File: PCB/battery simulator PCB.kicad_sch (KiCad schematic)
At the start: 9 parts

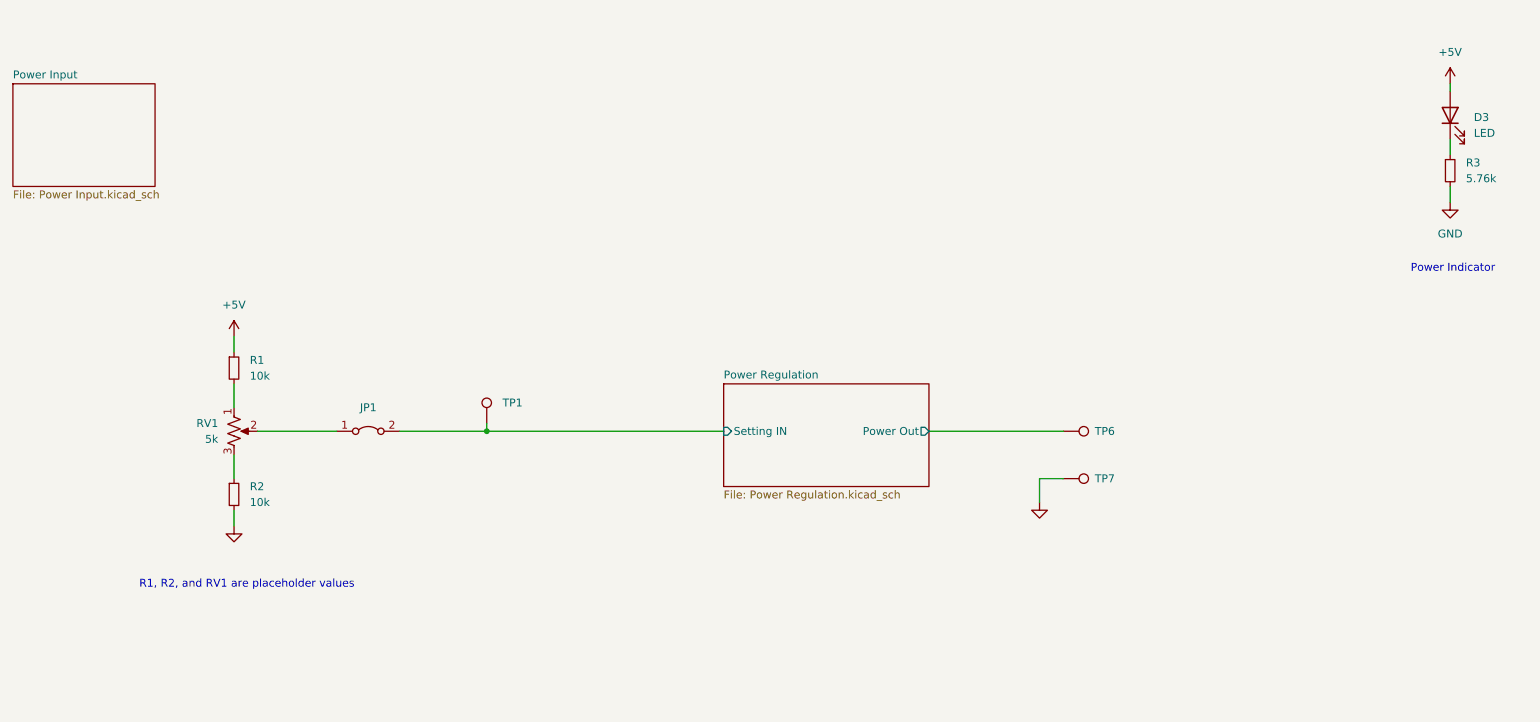
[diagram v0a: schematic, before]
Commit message: Added FUSB302B and associated circuitry.
Added FUSB302B, along with USB-C Connector and LDO.  The LDO is
needed to power the FUSB302B from the cable.

Also added some debugging and convenience items such as a QWIIC
connector and some test points.
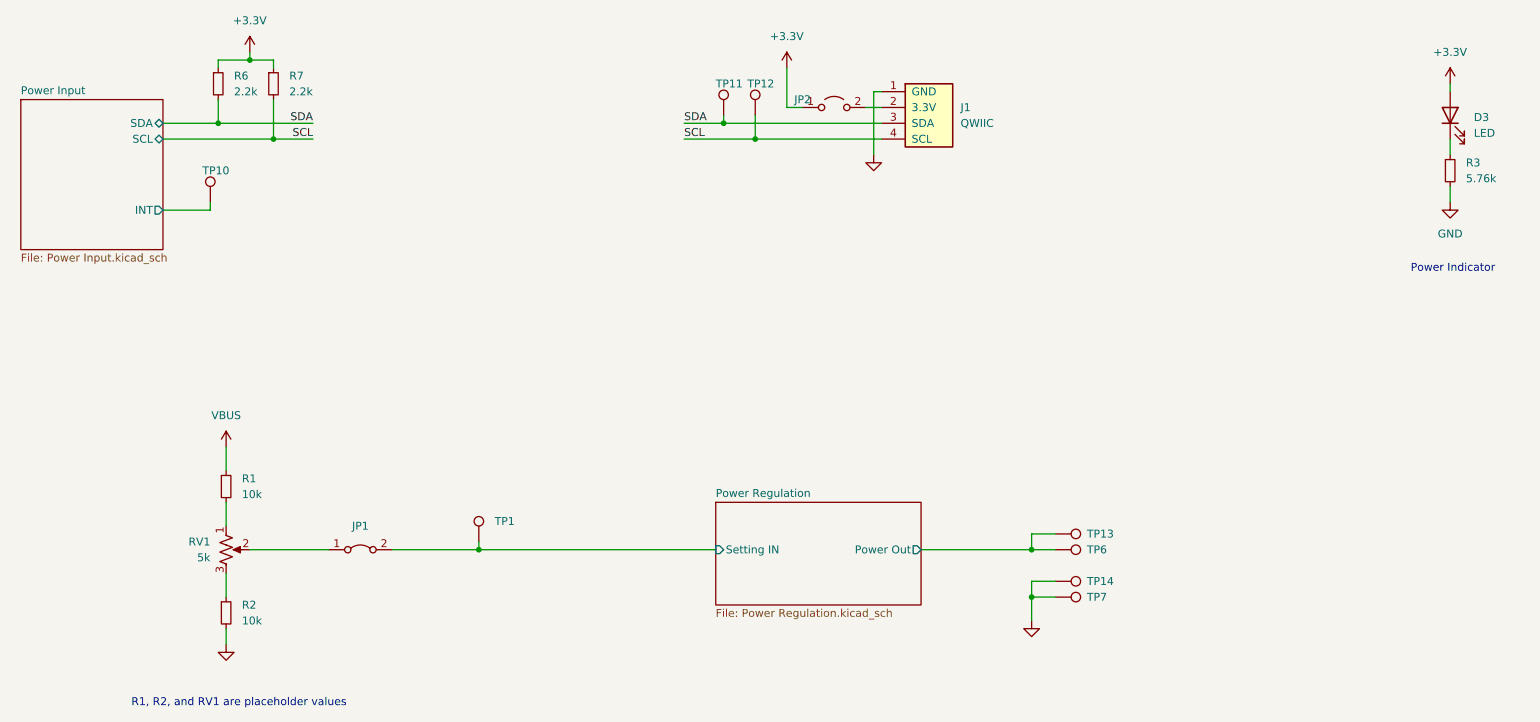
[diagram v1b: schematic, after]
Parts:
- added J1: QWIIC, Connector_JST:JST_SH_SM04B-SRSS-TB_1x04-1MP_P1.00mm_Horizontal, symbol battery simulator:QWIIC
- added JP2: Jumper_2_Open, Connector_PinHeader_2.54mm:PinHeader_1x02_P2.54mm_Vertical, symbol Jumper:Jumper_2_Open
- added R6, R7: 2.2k, Resistor_SMD:R_0402_1005Metric_Pad0.72x0.64mm_HandSolder, symbol Device:R_Small
- added TP10, TP11, TP12: TestPoint, TestPoint:TestPoint_Keystone_5010-5014_Multipurpose, symbol Connector:TestPoint
- added TP13, TP14: TestPoint, Connector_Wire:SolderWire-1sqmm_1x01_D1.4mm_OD2.7mm, symbol Connector:TestPoint
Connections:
- net GND: now also J1.1 (GND), TP14.1
- net Power Regulation/Power Out: now also TP13.1
- net +5V renamed +3.3V
- net +3.3V: now also JP2.1 (A), R6.1, R7.1; no longer R1.1
- new net: J1.2 (3.3V), JP2.2 (B)
- new net Power Input/INT: TP10.1
- new net SCL: J1.4 (SCL), R7.2, TP12.1
- new net SDA: J1.3 (SDA), R6.2, TP11.1
- new net VBUS: R1.1
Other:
- sheet Power Input ports: added INT, SCL, SDA; removed none
- moved on the sheet: JP1, R1, R2, RV1, TP1, TP6, TP7

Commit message: Update to KiCAD v7, and finalize for V1 build
Updated to KiCAD v7, which touched many files.

Also made some changes to finalize board for prototype build.  Simplified the
circuit a bit to just something built and tested.
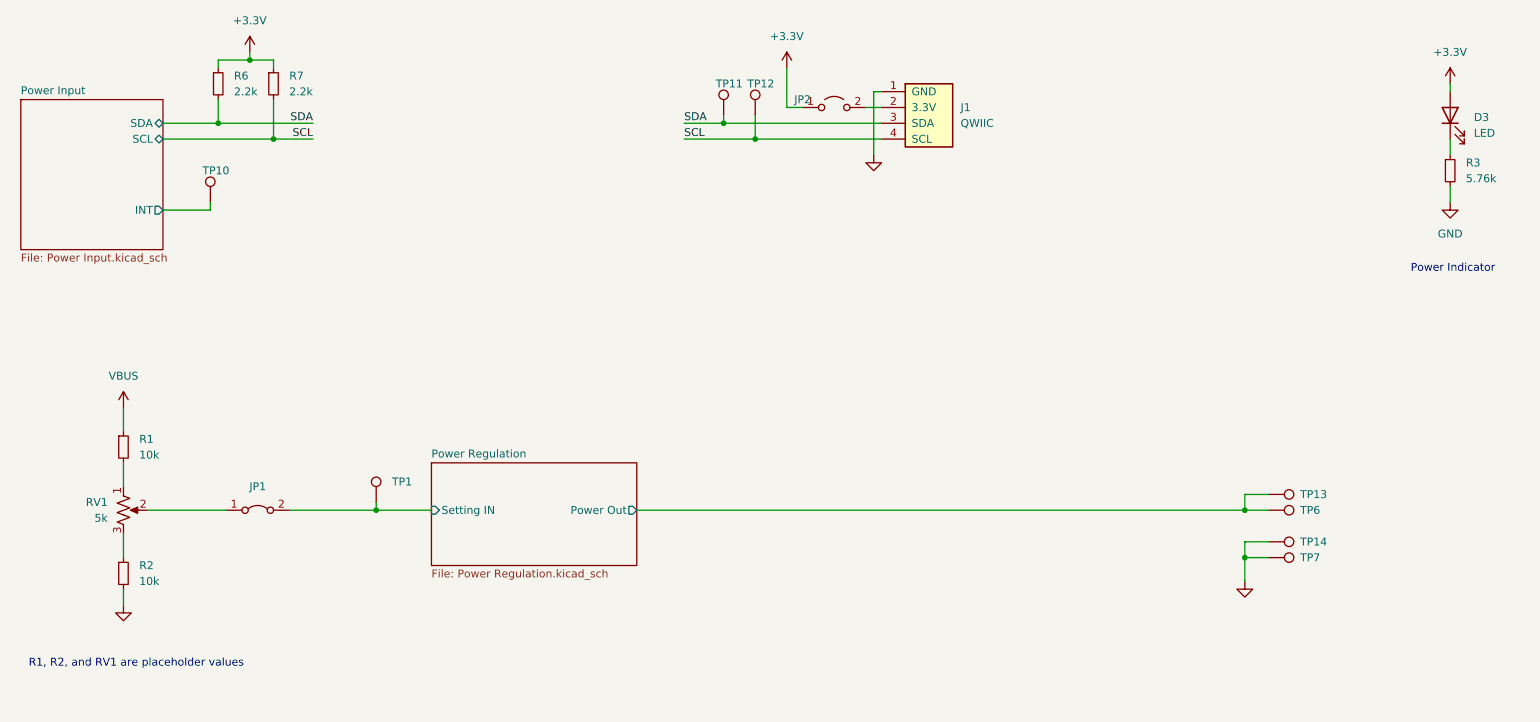
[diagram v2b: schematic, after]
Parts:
- RV1: footprint Potentiometer_THT:Potentiometer_Bourns_3386C_Horizontal -> Potentiometer_THT:Potentiometer_Bourns_3296W_Vertical
- TP1, TP10, TP11, TP12: footprint TestPoint:TestPoint_Keystone_5010-5014_Multipurpose -> TestPoint:TestPoint_Keystone_5000-5004_Miniature
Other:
- moved on the sheet: JP1, R1, R2, RV1, TP1, TP13, TP14, TP6, TP7
